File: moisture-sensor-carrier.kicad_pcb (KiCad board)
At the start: 4 copper layers, 42 x 155 mm, 61 parts, among them J1 USB-C receptacle, J2 Battery - Adafruit 1578, J3 Solar panel, J4 SWD 10p 1.27mm, J5 U.FL-R-SMT-1(10) antenna, U1 nRF54L15-QFAA, U2 nPM1300-QEAA, U3 FDC1004, U4 SHT45-AD1F, U5 TPS7A1650 5V LDO, X1 CM8V-T1A 32.768kHz CL=7pF 20p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, X2 FA-128 32MHz CL=8pF

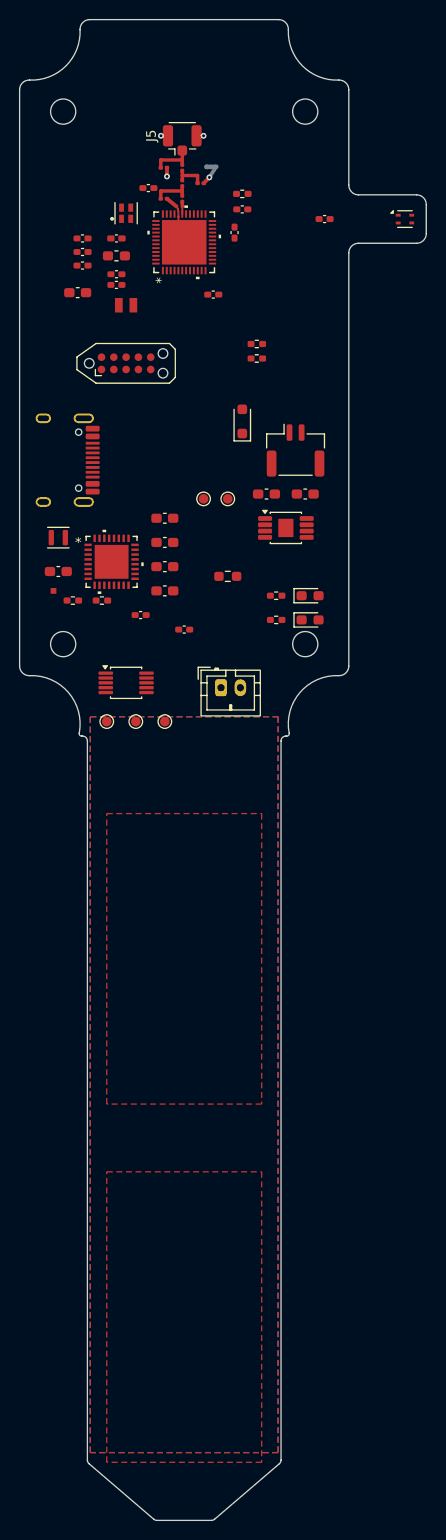
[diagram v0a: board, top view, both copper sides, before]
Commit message: Add the F.Cu ground pour, the In2.Cu +3V3 plane, and the sense-escape guard
Zone B had ground on In1.Cu only, so every one of the 51 F.Cu ground pads
needed its own via. ZoneB_GND_F collects them instead and ZoneB_3V3 does the
same for the 21 pads on /+3V3 - LAYOUT.md section 1 already assigns In2.Cu the
role 'power / guard pour' and this is the power half.

Kept off the RF: RFPourKeepout bans F.Cu pour within 1.1 mm of the x = 76.8
microstrip, because W = 0.36 mm comes from the MICROSTRIP equation and coplanar
ground beside the trace would pull the impedance down.

Sense: SenseNoGround carves In1.Cu away over the U3 -> Zone C escape, since
ground under a sense trace is measured capacitance, and SenseEscape_GUARD fills
what the carve left with driven guard instead.

Two DRU rules for fine-pitch fanout, with a trap worth naming: insideArea() is
true for a ZONE that merely OVERLAPS the area, so without the Type guards the
clearance exemption caught ZoneB_GND_F and through it every track and via on
the board - 97 violations nowhere near a QFN. tools_dru_test.py now carries a
containment case that fails if the exemption escapes its windows again.

124 -> 63 unconnected. 19/19 fire-tests.

Co-Authored-By: Claude Opus 5 <noreply@anthropic.com>
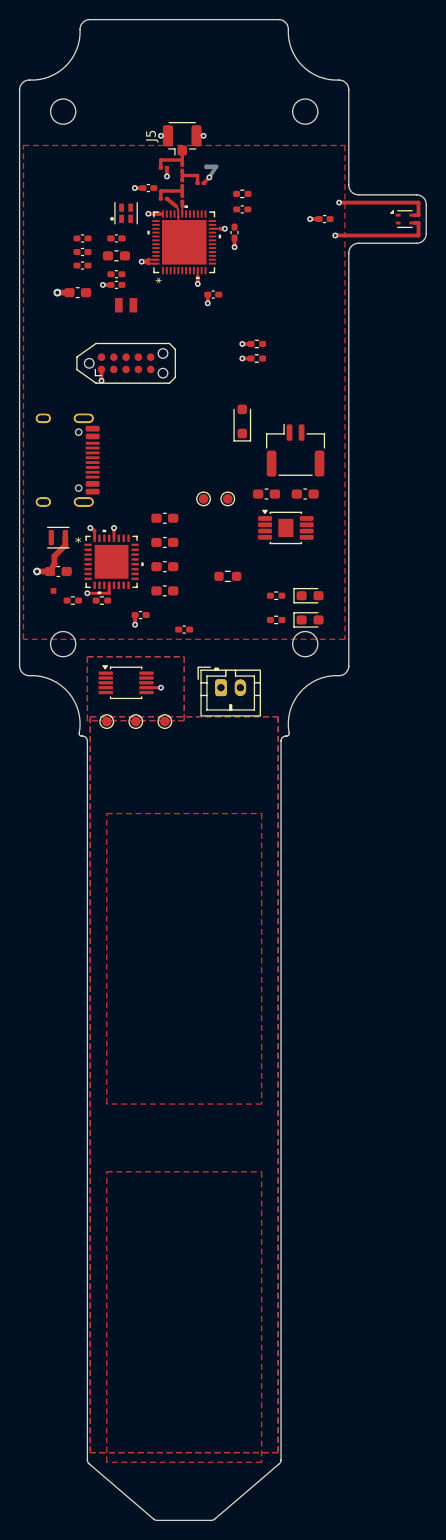
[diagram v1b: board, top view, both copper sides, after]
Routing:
- net /+3V3: track 0.00 -> 37.8 mm, vias 0 -> 19
- net GND: track 0.90 -> 13.1 mm, vias 3 -> 5
- added copper zone on In2.Cu, net /+3V3
- added copper zone on F.Cu, net GND

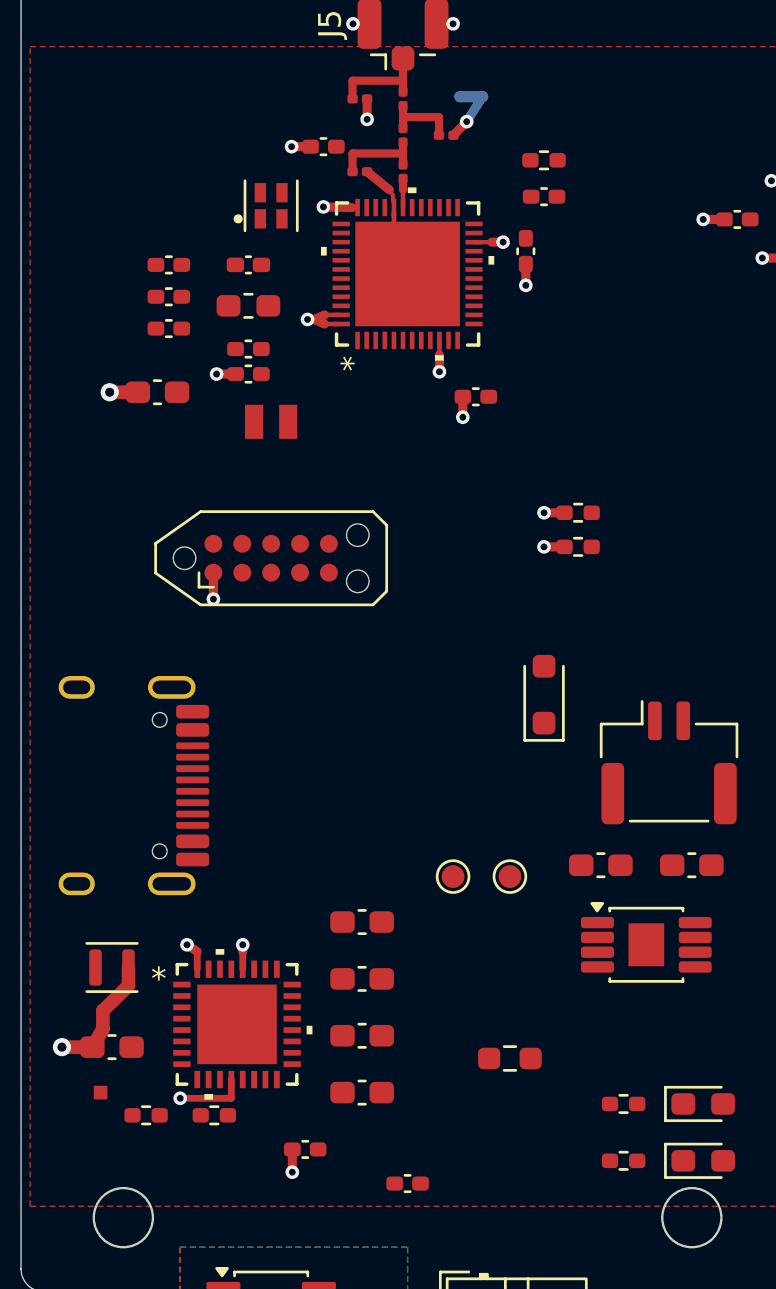
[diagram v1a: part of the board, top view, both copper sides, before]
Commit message: Route the nRF54L15 cluster; move C6 under pin 32 to unblock the escape
The blocker: U1 pins 33 (DECRF), 34 (XC1) and 35 (XC2) all escape westward
through the band between C6 and the bottom pad row, and /GND_PA ran diagonally
from C6.2 at (75.22, 58.5) up to pad 32 straight across it. Solving the
point-to-line distance for pin 33 at x = 76.0 gives a legal 0.15 mm track only
at y >= 59.814 or y <= 58.459 - inside the pad row, or the far side of
/GND_PA. Pin 33 had no legal escape at any width.

C6 is now rotated 270 deg at (76.10, 57.50), in the 0.91 mm gap between L3 and
L2, with its ground pad under pin 32. /GND_PA becomes a straight climb up
x = 76.35 and the corridor opens from y 57.7 to 59.698.

It also fixes an RF error that was already there. C6's shunt stub to the L2/L3
node was 3.02 mm, about 2 nH in series with 1.5 pF: at 2.4 GHz that turns
-j44.2 into -j14.0, a 3x error, so the stub was doing more to the match than
the capacitor. The stub is now 0.39 mm and the shunt reads -j39.7. The cost is
/GND_PA narrowing from 0.4 to 0.2 mm, about +0.7 nH in the VSS_PA return.

L10 and L1 both turned end for end so the switching node gets the direct path
and the quiet node takes the detour - Nordic's reference does the same.

The five long debug runs go on B.Cu as parallel lanes down the east side,
peeling west one at a time below J4. The lane order is forced: after a lane
turns west it runs north to its via, so the shallowest peel must have the
easternmost destination.

124 -> 45 unconnected, 0 DRC violations, 19/19 fire-tests.

Co-Authored-By: Claude Opus 5 <noreply@anthropic.com>
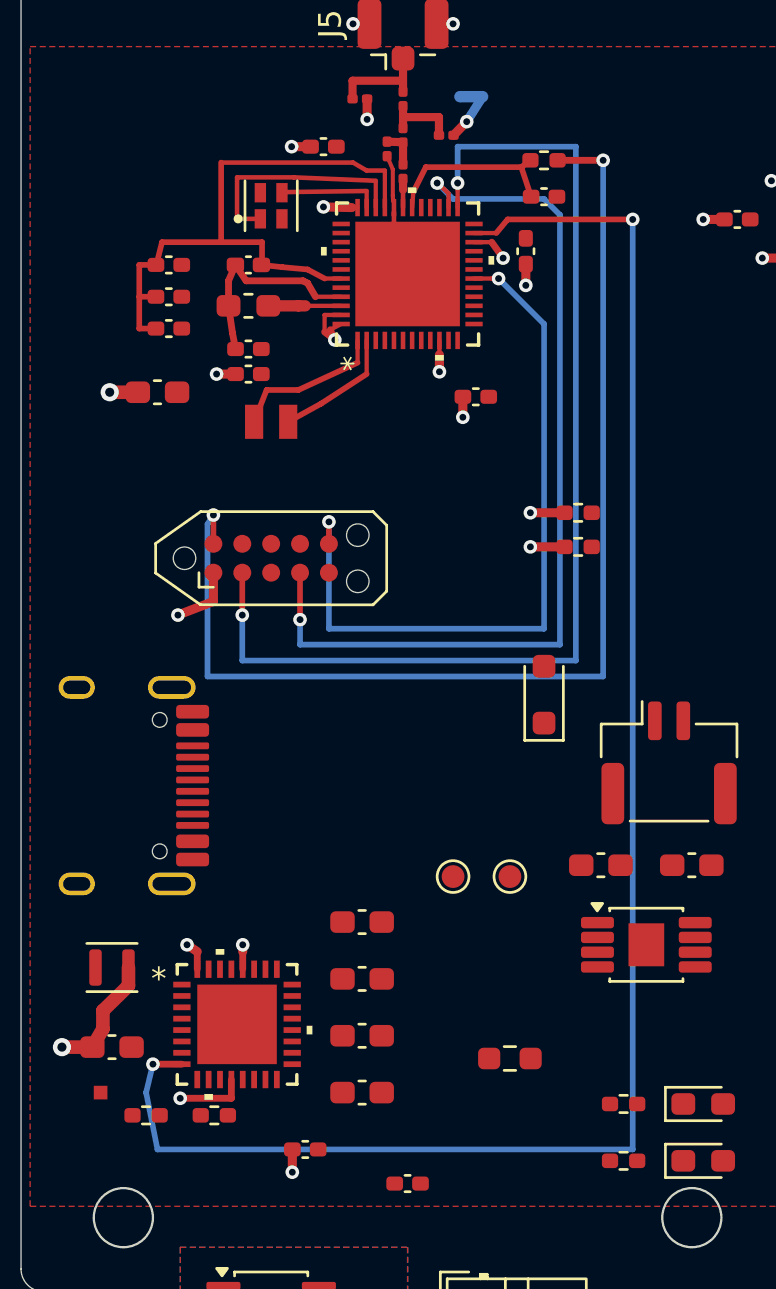
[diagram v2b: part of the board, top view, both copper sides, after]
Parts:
- moved C6 1.56 mm to (76.1, 57.5), turned to -90 degrees
- turned L1 to 180 degrees
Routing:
- net /PMIC_INT: track 0.00 -> 74.2 mm, vias 0 -> 2
- net /SWD_RST: track 0.00 -> 50.5 mm, vias 0 -> 2
- net /SWDIO: track 0.00 -> 49.0 mm, vias 0 -> 2
- net /SWDCLK: track 0.00 -> 40.8 mm, vias 0 -> 2
- net /P2.07_SWO: track 0.00 -> 32.4 mm, vias 0 -> 2
- net /DECA: track 0.00 -> 27.5 mm
- net /XC1: track 0.00 -> 10.1 mm
- net /DECD: track 0.00 -> 9.18 mm
- net /NRESET: track 0.00 -> 7.98 mm
- net /XL1: track 0.00 -> 6.75 mm
- net /XL2: track 0.00 -> 5.52 mm
- net /XC2: track 0.00 -> 4.48 mm
- net /+3V3: track 37.8 -> 41.5 mm
- net /DCC: track 0.00 -> 3.20 mm
- net /RF_A: track 3.98 -> 1.51 mm

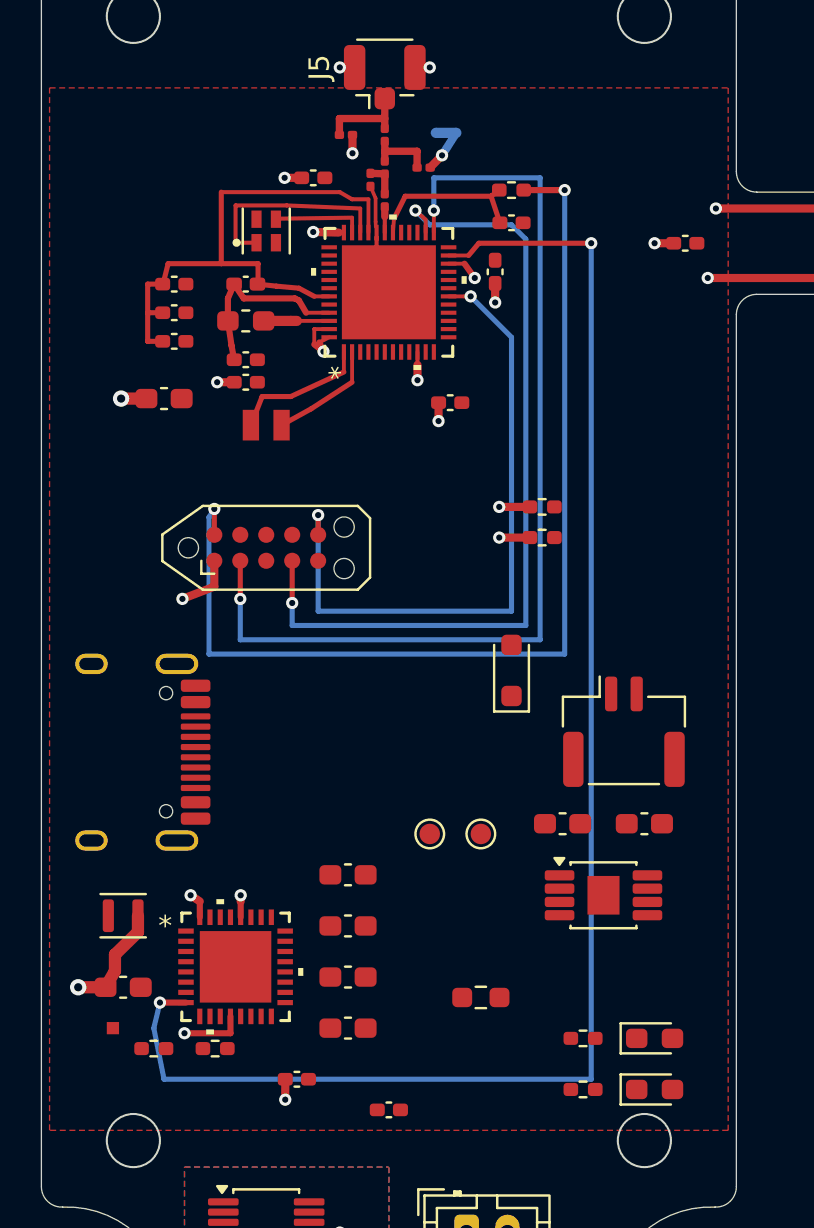
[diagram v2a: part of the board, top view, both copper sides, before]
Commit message: Add the QFN centre-pad via arrays and the ground stitching
U1 pad 49 gets a 4x4 grid at 1.2 mm pitch, which is what Nordic's QFAA
reference layout uses; U2 pad 33 gets 3x3 at the same pitch, because 4x4 at
1.0 mm would put the outer annulus past the 3.5 mm pad edge. 0.3 mm drill on
1.2 mm pitch is 0.9 mm hole to hole against the 0.5 mm minimum.

ORDER WITH VIAS TENTED. The paste is already window-paned to 66 % coverage,
and untented vias under a thermal pad wick solder out of the joint.

NT1 still bridges /GND_PA to GND alone: the array is GND throughout and its
nearest via sits 0.345 mm from NT1's /GND_PA pad.

109 stitching vias on a 2.5 mm grid tie ZoneB_GND_F through to the In1.Cu
plane. tools_stitch_gen.py generates the list by filtering the grid against
every pad, body, track and via on the board plus four banned regions - the RF
corridor above all, where perforating the plane under the microstrip is
exactly what must not happen. It reads the routed board, so it runs AFTER
routing, not before.

Two fire-tests had silently stopped testing anything. gndpa_via injected its
via inside the SHT45_Jut keepout, and KiCad reports one items_not_allowed per
item, so the keepout masked the rule under test; gndpa_layer's B.Cu band is
now under the debug bus. Both moved to Zone A, and both fire again.

Co-Authored-By: Claude Opus 5 <noreply@anthropic.com>
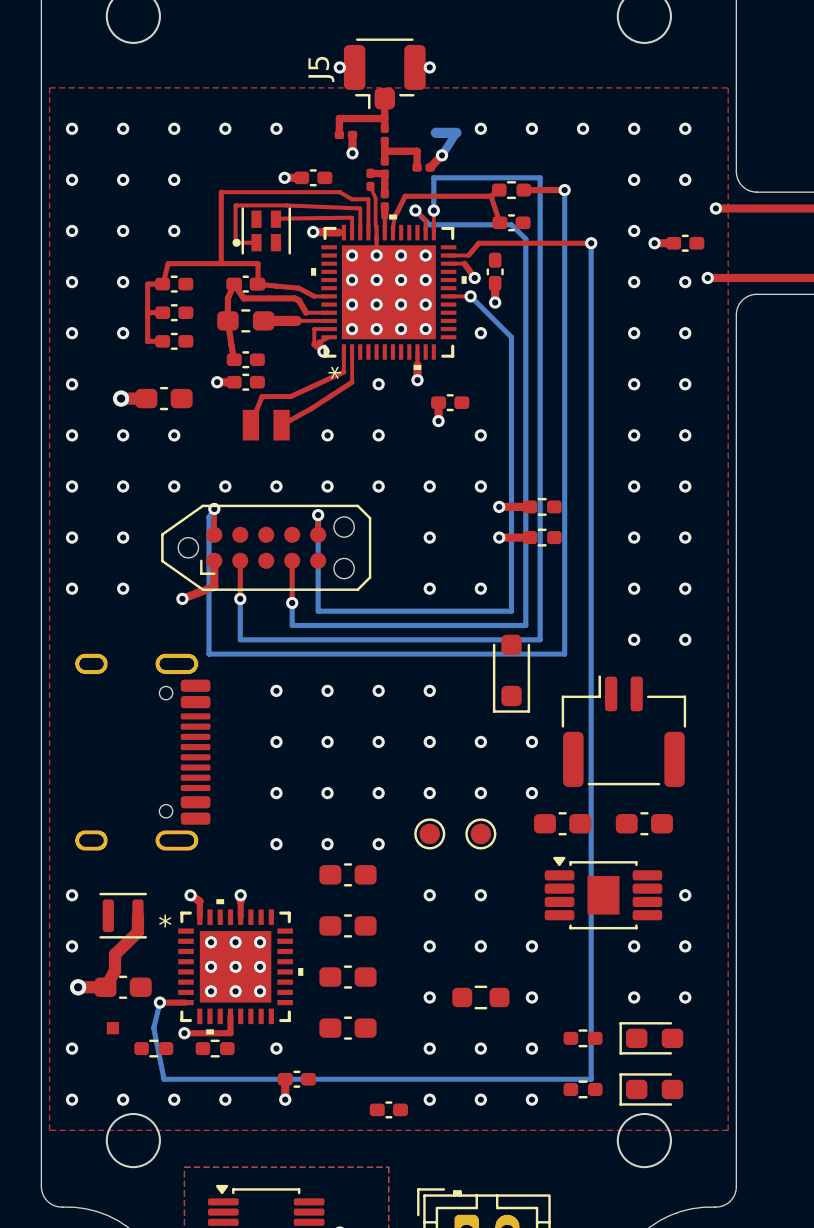
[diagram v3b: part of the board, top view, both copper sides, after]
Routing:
- net GND: vias 5 -> 139

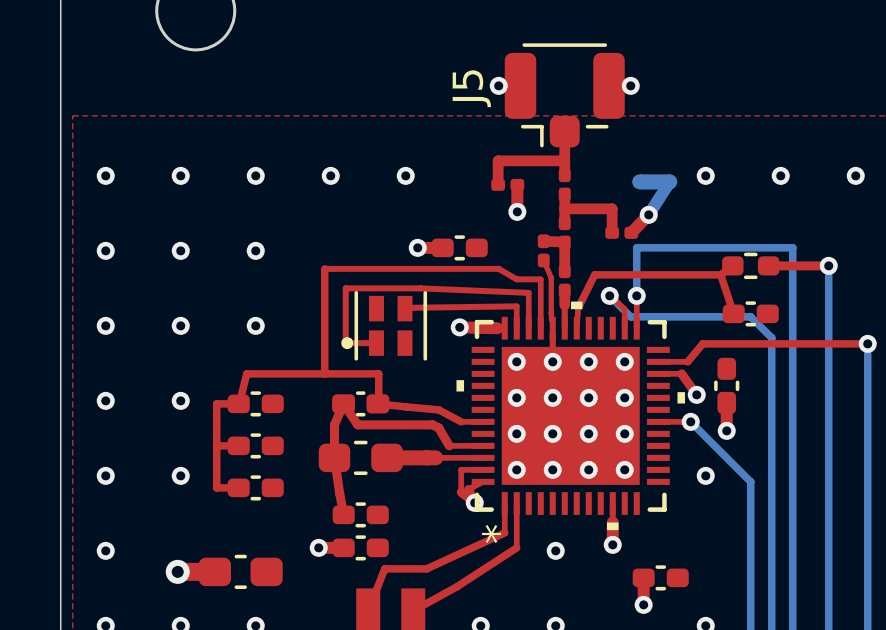
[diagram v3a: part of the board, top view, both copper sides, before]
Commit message: Attach the missing 3D models, and fix X2's pad numbering
X2's footprint had its pad numbering on the wrong diagonal, and it would have
stopped the 32 MHz oscillator starting.

The FA-128 datasheet puts the resonator between #1 and #3 with #2 and #4 on the
cover, and Epson's recommended land is 1.45 x 2.00 - the part seats with its
2.0 mm axis vertical, which puts the crystal terminals on the TL-BR diagonal
either way round, because 180 degrees maps a diagonal to itself. The footprint
had 1 and 3 on BL-TR, the cover diagonal, so XC1 and XC2 would have landed on
the grounded cover and the crystal terminals would have been tied to GND.

Nothing in ERC or DRC can see that: all four pads exist, all four are
connected, and the two ground pads are legitimately ground. It surfaced only
because the 3D model's index mark refused to line up with the footprint's.

Fixed in both the library and the placed instance - numbering rotated one
position, silk pin-1 dot moved, and the F.Fab rectangle transposed from 2.0 x
1.6 to 1.6 x 2.0 to agree with its own pads. /XC1 and /XC2 re-routed.

Renaming a pad does not move its net: the net follows the copper, so the first
pass left GND on pads 1 and 3 - the same defect one corner round. The script
now states the schematic's pad-to-net binding explicitly.

Models: U1 and U2 were already on disk in lib/nordic/, shipped with the vendor
footprints and never referenced; they need no rotation because they are
authored for KiCad's frame. X1 and X2 are vendor exports with the package
height along +Y and take one 90 degree turn about X - measured with cadquery,
not guessed, and verified with kicad-cli pcb render.

DRC 0 errors, ERC 0, 19/19 fire-tests, 44 unconnected unchanged.

Co-Authored-By: Claude Opus 5 <noreply@anthropic.com>
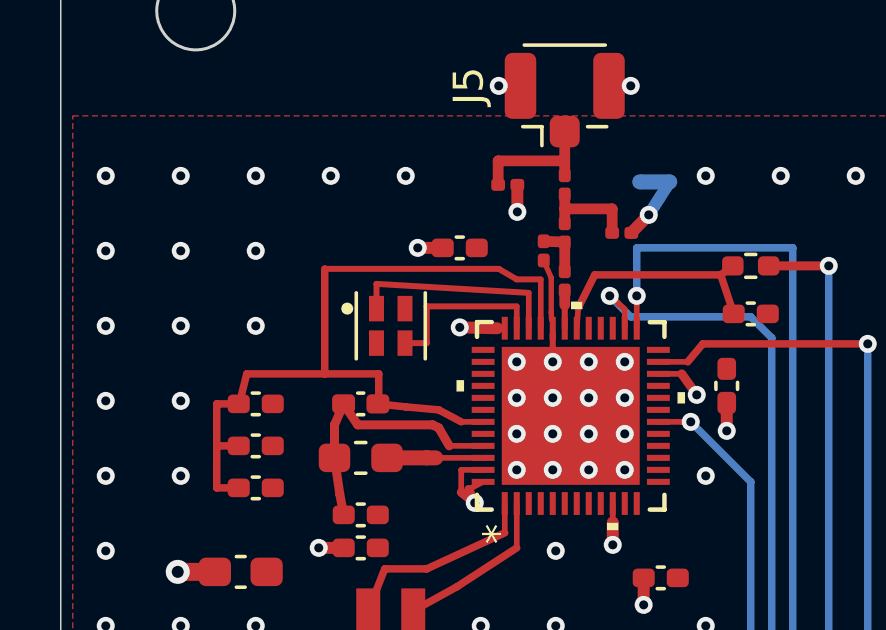
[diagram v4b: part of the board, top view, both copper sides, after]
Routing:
- net /XC1: track 10.1 -> 7.09 mm
- net /XC2: track 4.48 -> 5.68 mm
